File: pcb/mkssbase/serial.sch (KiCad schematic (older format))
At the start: 20 parts, among them IC3 MAX485E, IC4 AMS1117-3.3, J10 TO_J7, J11 24V PWR, J12 LED LIGHTING, J13 AIR VALVE, J14 AIMING LASER, J5 POWEROFF, J9 CHILLER SERIAL, Q1 ZXMN4A06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

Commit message: Fix footprints.
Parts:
- C10, C11, C8, C9: footprint SMD_Packages:SMD-1206_Pol -> Capacitor_SMD:CP_Elec_4x3
- C7: footprint Capacitors_SMD:C_0805 -> Capacitor_SMD:C_0805_2012Metric
- D1: footprint Diodes_SMD:D_SMA_Standard -> Diode_SMD:D_SMA
- IC3: footprint (none) -> Package_SO:SOIC-8_3.9x4.9mm_P1.27mm
- J10: footprint Connectors:PINHEAD1-6 -> Connector_JST:JST_XH_B06B-XH-A_1x06_P2.50mm_Vertical
- J11, J12, J13, J14, J9: footprint Connectors_JST:JST_PH_B2B-PH-K_02x2.00mm_Straight -> Connector_JST:JST_PH_B2B-PH-K_1x02_P2.00mm_Vertical
- J5: footprint Connectors_JST:JST_PH_B3B-PH-K_03x2.00mm_Straight -> Connector_JST:JST_PH_B3B-PH-K_1x03_P2.00mm_Vertical
- Q1: footprint (none) -> Package_TO_SOT_SMD:SOT-223-3_TabPin2
- R10, R11, R12: footprint Resistors_SMD:R_0603 -> Resistor_SMD:R_0603_1608Metric
- U1: value buck-converter -> MP1584 module; footprint mylib:buck-converter -> mkssbase:MP1584-module
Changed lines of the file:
@@
 F 0 "J9" H 4000 2300 50  0000 C CNN
 F 1 "CHILLER SERIAL" V 4100 2150 50  0000 C CNN
-F 2 "Connectors_JST:JST_PH_B2B-PH-K_02x2.00mm_Straight" H 4000 2150 50  0001 C CNN
+F 2 "Connector_JST:JST_PH_B2B-PH-K_1x02_P2.00mm_Vertical" H 4000 2150 50  0001 C CNN
 F 3 "" H 4000 2150 50  0001 C CNN
 	1    4000 2150
@@
 F 0 "C7" H 2075 3350 50  0000 L CNN
 F 1 "100n" H 2075 3150 50  0000 L CNN
-F 2 "Capacitors_SMD:C_0805" H 2088 3100 50  0001 C CNN
+F 2 "Capacitor_SMD:C_0805_2012Metric" H 2088 3100 50  0001 C CNN
 F 3 "" H 2050 3250 50  0001 C CNN
 	1    2050 3250
@@
 F 0 "R10" V 3680 2500 50  0000 C CNN
 F 1 "120R" V 3600 2500 50  0000 C CNN
-F 2 "Resistors_SMD:R_0603" V 3530 2500 50  0001 C CNN
+F 2 "Resistor_SMD:R_0603_1608Metric" V 3530 2500 50  0001 C CNN
 F 3 "" H 3600 2500 50  0001 C CNN
 	1    3600 2500
@@
 F 0 "C8" H 6325 2500 50  0000 L CNN
 F 1 "100u" H 6325 2300 50  0000 L CNN
-F 2 "SMD_Packages:SMD-1206_Pol" H 6338 2250 50  0001 C CNN
+F 2 "Capacitor_SMD:CP_Elec_4x3" H 6338 2250 50  0001 C CNN
 F 3 "" H 6300 2400 50  0001 C CNN
 	1    6300 2400
@@
 F 0 "C9" H 7475 2500 50  0000 L CNN
 F 1 "100u" H 7475 2300 50  0000 L CNN
-F 2 "SMD_Packages:SMD-1206_Pol" H 7488 2250 50  0001 C CNN
+F 2 "Capacitor_SMD:CP_Elec_4x3" H 7488 2250 50  0001 C CNN
 F 3 "" H 7450 2400 50  0001 C CNN
 	1    7450 2400
@@
 F 0 "J10" H 3100 5050 50  0000 C CNN
 F 1 "TO_J7" V 3200 4700 50  0000 C CNN
-F 2 "Connectors:PINHEAD1-6" H 3100 4700 50  0001 C CNN
+F 2 "Connector_JST:JST_XH_B06B-XH-A_1x06_P2.50mm_Vertical" H 3100 4700 50  0001 C CNN
 F 3 "" H 3100 4700 50  0001 C CNN
 	1    3100 4700
@@
 F 0 "J5" H 1500 4400 50  0000 C CNN
 F 1 "POWEROFF" V 1600 4200 50  0000 C CNN
-F 2 "Connectors_JST:JST_PH_B3B-PH-K_03x2.00mm_Straight" H 1500 4200 50  0001 C CNN
+F 2 "Connector_JST:JST_PH_B3B-PH-K_1x03_P2.00mm_Vertical" H 1500 4200 50  0001 C CNN
 F 3 "" H 1500 4200 50  0001 C CNN
 	1    1500 4200
@@
 F 0 "J11" H 5050 3650 50  0000 C CNN
 F 1 "24V PWR" V 5150 3500 50  0000 C CNN
-F 2 "Connectors_JST:JST_PH_B2B-PH-K_02x2.00mm_Straight" H 5050 3500 50  0001 C CNN
+F 2 "Connector_JST:JST_PH_B2B-PH-K_1x02_P2.00mm_Vertical" H 5050 3500 50  0001 C CNN
 F 3 "" H 5050 3500 50  0001 C CNN
 	1    5050 3500
@@
 F 0 "J12" H 7600 3650 50  0000 C CNN
 F 1 "LED LIGHTING" V 7700 3500 50  0000 C CNN
-F 2 "Connectors_JST:JST_PH_B2B-PH-K_02x2.00mm_Straight" H 7600 3500 50  0001 C CNN
+F 2 "Connector_JST:JST_PH_B2B-PH-K_1x02_P2.00mm_Vertical" H 7600 3500 50  0001 C CNN
 F 3 "" H 7600 3500 50  0001 C CNN
 	1    7600 3500
@@
 F 0 "C10" H 5725 3800 50  0000 L CNN
 F 1 "100u" H 5725 3600 50  0000 L CNN
-F 2 "SMD_Packages:SMD-1206_Pol" H 5738 3550 50  0001 C CNN
+F 2 "Capacitor_SMD:CP_Elec_4x3" H 5738 3550 50  0001 C CNN
 F 3 "" H 5700 3700 50  0001 C CNN
 	1    5700 3700
@@
 F 0 "J13" H 7600 4300 50  0000 C CNN
 F 1 "AIR VALVE" V 7700 4150 50  0000 C CNN
-F 2 "Connectors_JST:JST_PH_B2B-PH-K_02x2.00mm_Straight" H 7600 4150 50  0001 C CNN
+F 2 "Connector_JST:JST_PH_B2B-PH-K_1x02_P2.00mm_Vertical" H 7600 4150 50  0001 C CNN
 F 3 "" H 7600 4150 50  0001 C CNN
 	1    7600 4150
@@
 F 0 "C11" H 6925 3800 50  0000 L CNN
 F 1 "100u" H 6925 3600 50  0000 L CNN
-F 2 "SMD_Packages:SMD-1206_Pol" H 6938 3550 50  0001 C CNN
+F 2 "Capacitor_SMD:CP_Elec_4x3" H 6938 3550 50  0001 C CNN
 F 3 "" H 6900 3700 50  0001 C CNN
 	1    6900 3700
@@
 F 0 "D1" H 7150 4550 50  0000 C CNN
 F 1 "SS34" H 7150 4350 50  0000 C CNN
-F 2 "Diodes_SMD:D_SMA_Standard" H 7150 4450 50  0001 C CNN
+F 2 "Diode_SMD:D_SMA" H 7150 4450 50  0001 C CNN
 F 3 "" H 7150 4450 50  0001 C CNN
 	1    7150 4450
@@
 F 0 "R12" V 6680 5000 50  0000 C CNN
 F 1 "22R" V 6600 5000 50  0000 C CNN
-F 2 "Resistors_SMD:R_0603" V 6530 5000 50  0001 C CNN
+F 2 "Resistor_SMD:R_0603_1608Metric" V 6530 5000 50  0001 C CNN
 F 3 "" H 6600 5000 50  0001 C CNN
 	1    6600 5000
@@
 F 0 "R11" V 6380 5200 50  0000 C CNN
 F 1 "10K" V 6300 5200 50  0000 C CNN
-F 2 "Resistors_SMD:R_0603" V 6230 5200 50  0001 C CNN
+F 2 "Resistor_SMD:R_0603_1608Metric" V 6230 5200 50  0001 C CNN
 F 3 "" H 6300 5200 50  0001 C CNN
 	1    6300 5200
@@
 F 0 "J14" H 1500 6200 50  0000 C CNN
 F 1 "AIMING LASER" V 1600 6050 50  0000 C CNN
-F 2 "Connectors_JST:JST_PH_B2B-PH-K_02x2.00mm_Straight" H 1500 6050 50  0001 C CNN
+F 2 "Connector_JST:JST_PH_B2B-PH-K_1x02_P2.00mm_Vertical" H 1500 6050 50  0001 C CNN
 F 3 "" H 1500 6050 50  0001 C CNN
 	1    1500 6050
@@
 F 0 "Q1" H 7255 5046 50  0000 L CNN
 F 1 "ZXMN4A06" H 7255 4955 50  0000 L CNN
-F 2 "" H 7250 5100 50  0001 C CNN
+F 2 "Package_TO_SOT_SMD:SOT-223-3_TabPin2" H 7250 5100 50  0001 C CNN
 F 3 "~" H 7050 5000 50  0001 C CNN
 	1    7050 5000
@@
 Wire Wire Line
 	7450 2150 7450 2250
-$Comp
-L buck-converter:buck-converter U1
-U 1 1 5C510D8B
-P 6300 3550
-F 0 "U1" H 6325 3865 50  0000 C CNN
-F 1 "buck-converter" H 6325 3774 50  0000 C CNN
-F 2 "mylib:buck-converter" H 6300 3300 50  0001 C CNN
-F 3 "" H 6300 3800 50  0001 C CNN
-	1    6300 3550
-	1    0    0    -1
-$EndComp
 Wire Wire Line
 	5700 3500 5950 3500
@@
 F 0 "IC3" H 2400 2700 50  0000 C CNN
 F 1 "MAX485E" H 2500 2600 50  0000 C CNN
-F 2 "" H 2900 1450 50  0001 C CNN
+F 2 "Package_SO:SOIC-8_3.9x4.9mm_P1.27mm" H 2900 1450 50  0001 C CNN
 F 3 "https://datasheets.maximintegrated.com/en/ds/MAX1487E-MAX491E.pdf" H 2900 2200 50  0001 C CNN
 	1    2900 2150
@@
 Wire Wire Line
 	3300 2050 3300 2150
+$Comp
+L buck-converter:buck-converter U1
+U 1 1 5C549011
+P 6300 3550
+F 0 "U1" H 6325 3865 50  0000 C CNN
+F 1 "MP1584 module" H 6325 3774 50  0000 C CNN
+F 2 "mkssbase:MP1584-module" H 6300 3300 50  0001 C CNN
+F 3 "" H 6300 3800 50  0001 C CNN
+	1    6300 3550
+	1    0    0    -1
+$EndComp
 $EndSCHEMATC

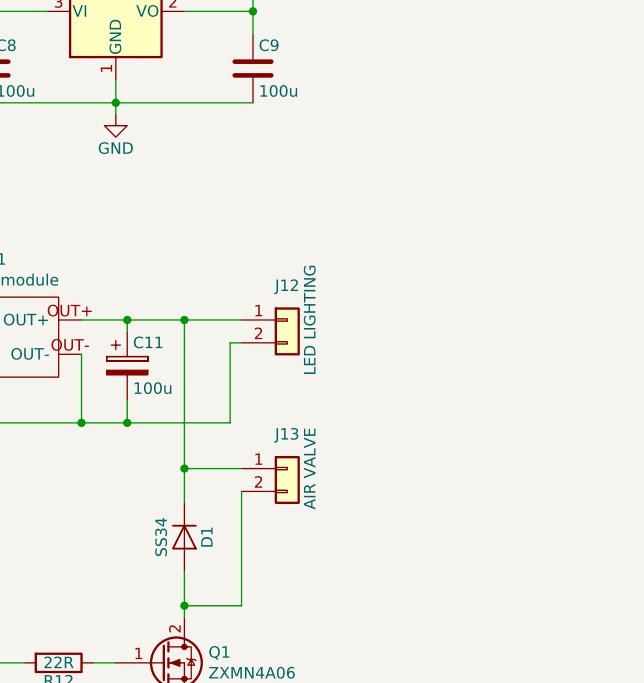
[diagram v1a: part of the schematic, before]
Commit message: Add chiller control.
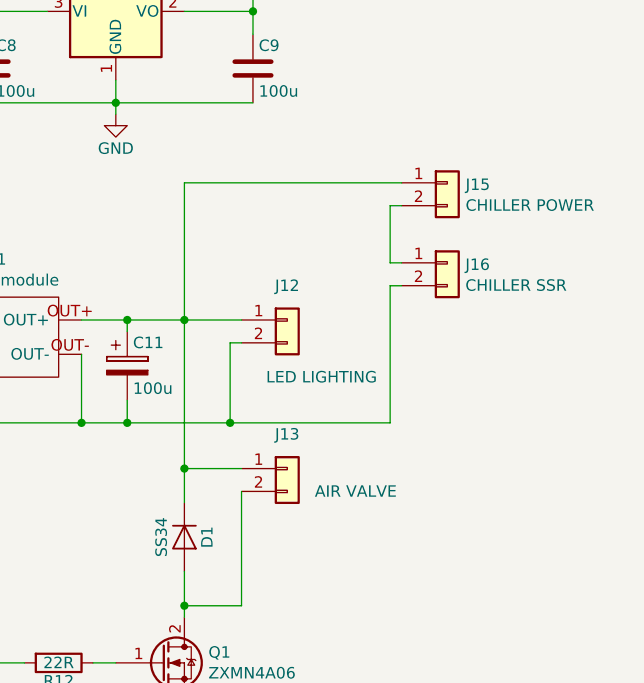
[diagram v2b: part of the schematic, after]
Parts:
- added J15: CHILLER POWER, Connector_JST:JST_PH_B2B-PH-K_1x02_P2.00mm_Vertical, symbol Connector_Generic:Conn_01x02
- added J16: CHILLER SSR, Connector_JST:JST_PH_B2B-PH-K_1x02_P2.00mm_Vertical, symbol Connector_Generic:Conn_01x02
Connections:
- net GND: now also J16.2 (Pin_2)
- net at C11.1, D1.1 (K), J12.1 (Pin_1)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: now also J15.1 (Pin_1)
- new net: J15.2 (Pin_2), J16.1 (Pin_1)
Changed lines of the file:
@@
 EESchema Schematic File Version 4
 LIBS:mkssbase-cache
+LIBS:chillercontrol-cache
 EELAYER 26 0
 EELAYER END
 $Descr A4 11693 8268
 encoding utf-8
-Sheet 2 2
+Sheet 2 3
 Title ""
 Date ""
@@
 AR Path="/58F3B713/58F4BA9B" Ref="J12"  Part="1"
 F 0 "J12" H 7600 3650 50  0000 C CNN
-F 1 "LED LIGHTING" V 7700 3500 50  0000 C CNN
+F 1 "LED LIGHTING" H 7750 3250 50  0000 C CNN
 F 2 "Connector_JST:JST_PH_B2B-PH-K_1x02_P2.00mm_Vertical" H 7600 3500 50  0001 C CNN
 F 3 "" H 7600 3500 50  0001 C CNN
@@
 AR Path="/58F3B713/58F4BF09" Ref="J13"  Part="1"
 F 0 "J13" H 7600 4300 50  0000 C CNN
-F 1 "AIR VALVE" V 7700 4150 50  0000 C CNN
+F 1 "AIR VALVE" H 7900 4050 50  0000 C CNN
 F 2 "Connector_JST:JST_PH_B2B-PH-K_1x02_P2.00mm_Vertical" H 7600 4150 50  0001 C CNN
 F 3 "" H 7600 4150 50  0001 C CNN
@@
 	1    0    0    -1
 $EndComp
+$Comp
+L Connector_Generic:Conn_01x02 J15
+U 1 1 5C57EF6D
+P 8300 2900
+F 0 "J15" H 8380 2892 50  0000 L CNN
+F 1 "CHILLER POWER" H 8380 2801 50  0000 L CNN
+F 2 "Connector_JST:JST_PH_B2B-PH-K_1x02_P2.00mm_Vertical" H 8300 2900 50  0001 C CNN
+F 3 "~" H 8300 2900 50  0001 C CNN
+	1    8300 2900
+	1    0    0    -1
+$EndComp
+$Comp
+L Connector_Generic:Conn_01x02 J16
+U 1 1 5C57EFEC
+P 8300 3250
+F 0 "J16" H 8379 3242 50  0000 L CNN
+F 1 "CHILLER SSR" H 8379 3151 50  0000 L CNN
+F 2 "Connector_JST:JST_PH_B2B-PH-K_1x02_P2.00mm_Vertical" H 8300 3250 50  0001 C CNN
+F 3 "~" H 8300 3250 50  0001 C CNN
+	1    8300 3250
+	1    0    0    -1
+$EndComp
+Wire Wire Line
+	8100 2900 7150 2900
+Wire Wire Line
+	7150 2900 7150 3500
+Wire Wire Line
+	8100 3000 8050 3000
+Wire Wire Line
+	8050 3000 8050 3250
+Wire Wire Line
+	8050 3250 8100 3250
+Wire Wire Line
+	7350 3950 8050 3950
+Wire Wire Line
+	8050 3950 8050 3350
+Wire Wire Line
+	8050 3350 8100 3350
+Connection ~ 7350 3950
 $EndSCHEMATC

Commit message: Integrate chiller control.
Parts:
- C10, C11, C8, C9: footprint Capacitor_SMD:CP_Elec_4x3 -> Capacitor_SMD:CP_Elec_10x10
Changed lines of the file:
@@
 EESchema Schematic File Version 4
 LIBS:mkssbase-cache
-LIBS:chillercontrol-cache
 EELAYER 26 0
 EELAYER END
@@
 F 0 "C8" H 6325 2500 50  0000 L CNN
 F 1 "100u" H 6325 2300 50  0000 L CNN
-F 2 "Capacitor_SMD:CP_Elec_4x3" H 6338 2250 50  0001 C CNN
+F 2 "Capacitor_SMD:CP_Elec_10x10" H 6338 2250 50  0001 C CNN
 F 3 "" H 6300 2400 50  0001 C CNN
 	1    6300 2400
@@
 F 0 "C9" H 7475 2500 50  0000 L CNN
 F 1 "100u" H 7475 2300 50  0000 L CNN
-F 2 "Capacitor_SMD:CP_Elec_4x3" H 7488 2250 50  0001 C CNN
+F 2 "Capacitor_SMD:CP_Elec_10x10" H 7488 2250 50  0001 C CNN
 F 3 "" H 7450 2400 50  0001 C CNN
 	1    7450 2400
@@
 F 0 "C10" H 5725 3800 50  0000 L CNN
 F 1 "100u" H 5725 3600 50  0000 L CNN
-F 2 "Capacitor_SMD:CP_Elec_4x3" H 5738 3550 50  0001 C CNN
+F 2 "Capacitor_SMD:CP_Elec_10x10" H 5738 3550 50  0001 C CNN
 F 3 "" H 5700 3700 50  0001 C CNN
 	1    5700 3700
@@
 F 0 "C11" H 6925 3800 50  0000 L CNN
 F 1 "100u" H 6925 3600 50  0000 L CNN
-F 2 "Capacitor_SMD:CP_Elec_4x3" H 6938 3550 50  0001 C CNN
+F 2 "Capacitor_SMD:CP_Elec_10x10" H 6938 3550 50  0001 C CNN
 F 3 "" H 6900 3700 50  0001 C CNN
 	1    6900 3700

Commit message: Add inverted laser control signal.
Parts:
- C7: footprint Capacitor_SMD:C_0805_2012Metric -> Capacitor_SMD:C_0603_1608Metric
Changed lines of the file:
@@
 $Descr A4 11693 8268
 encoding utf-8
-Sheet 2 3
+Sheet 2 2
 Title ""
 Date ""
@@
 F 0 "C7" H 2075 3350 50  0000 L CNN
 F 1 "100n" H 2075 3150 50  0000 L CNN
-F 2 "Capacitor_SMD:C_0805_2012Metric" H 2088 3100 50  0001 C CNN
+F 2 "Capacitor_SMD:C_0603_1608Metric" H 2088 3100 50  0001 C CNN
 F 3 "" H 2050 3250 50  0001 C CNN
 	1    2050 3250
